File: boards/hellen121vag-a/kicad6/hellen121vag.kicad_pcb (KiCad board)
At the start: 2 copper layers, 164 x 118 mm, 70 parts, among them J1 USB_B_Mini, M1 Module-can-0.1, M10 Module-can-0.1, M11 Module-vr-0.1, M12 Module-dinput4-0.1, M2 Module-power5-0.1, M3 Module-mcu-0.1, M4 Module-input-0.1, M5 Module-knock-0.1, M6 Module-output-0.1, M7 Module-ign8-0.1, M8 Module-power12-0.1, M9 Module-wbo-0.1, P1 368255-2

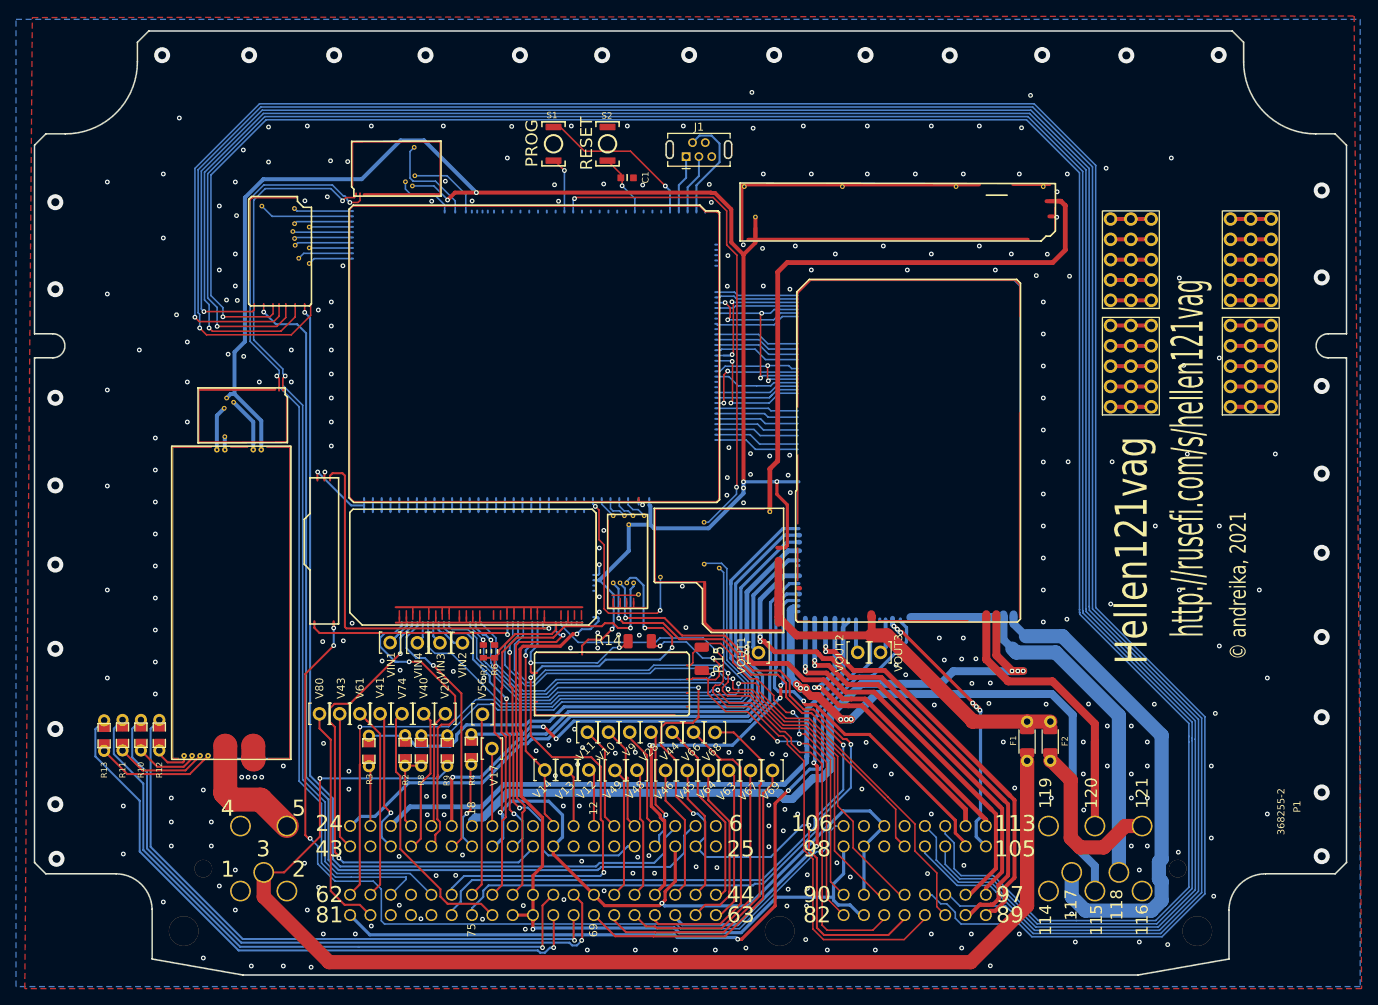
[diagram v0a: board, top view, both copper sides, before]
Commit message: Upd pcb, sch
Power5 0.2
turn connector
bridge driver is almost complete
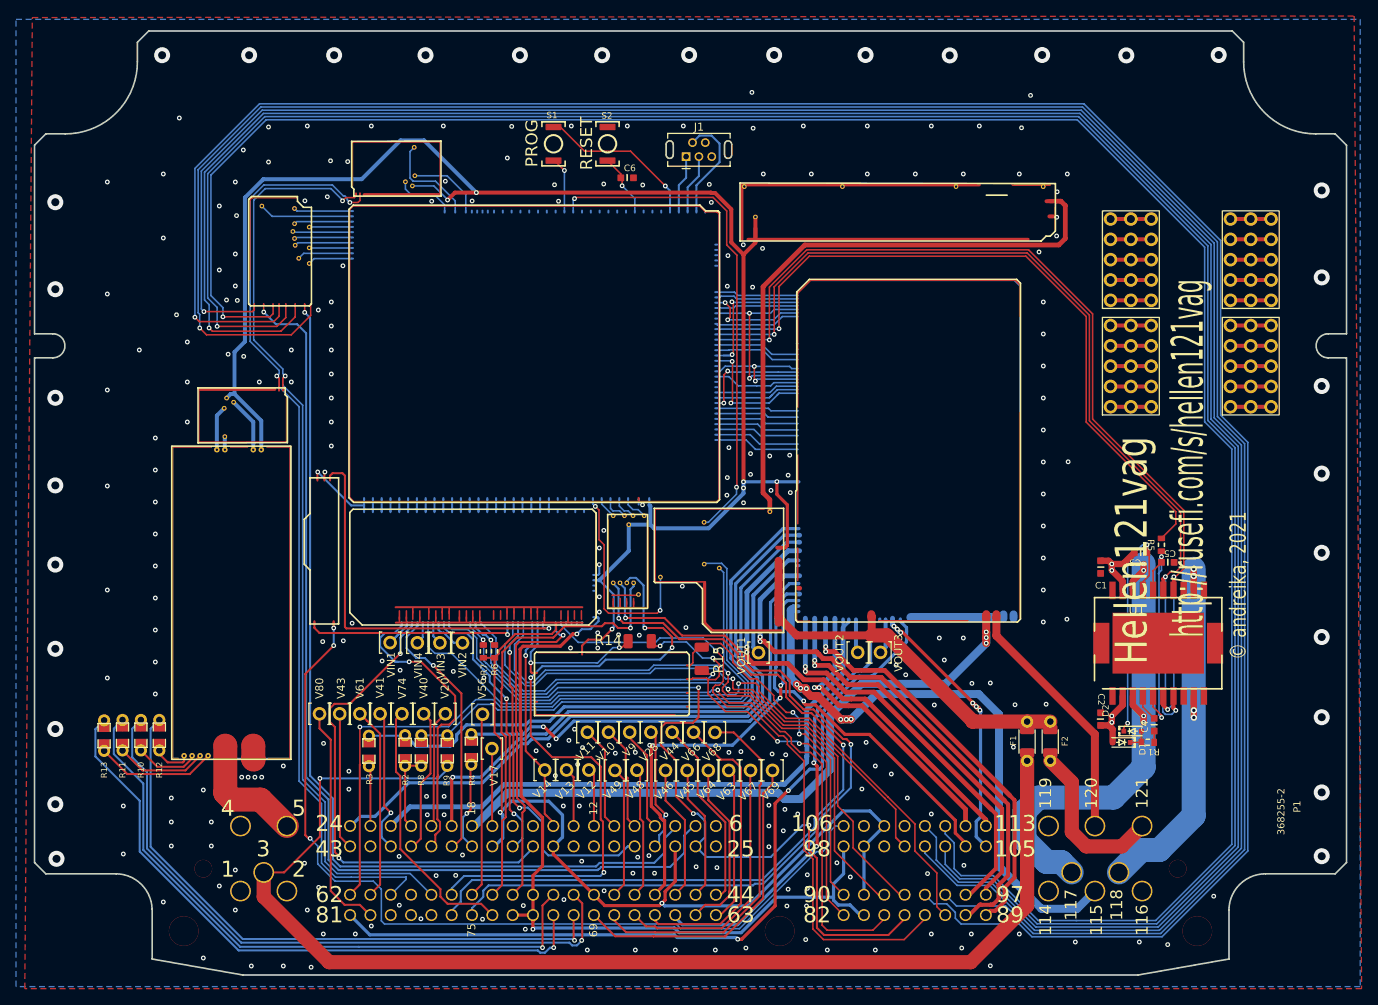
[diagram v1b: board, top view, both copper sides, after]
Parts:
- added C2: 100n, hellen-one-common:C0603, F.Cu at (179.0, 78.4)
- added C3: 220n, hellen-one-common:C0603, F.Cu at (184.0, 57.6)
- added C4: 10n, hellen-one-common:C0603, F.Cu at (185.7, 79.1)
- added C5: 5.6n, hellen-one-common:C0603, F.Cu at (187.4, 58.8)
- added C6: 100n, hellen-one-common:C0603, F.Cu at (119.8, 10.7)
- added D1: 1N4148WS, hellen-one-common:SOD-323, F.Cu at (181.6, 81.3)
- added D2: 1N4148WS, hellen-one-common:SOD-323, F.Cu at (183.0, 79.9)
- added R1: 100, hellen-one-common:R0603, F.Cu at (184.9, 81.3)
- added R5: 100k, hellen-one-common:R0603, F.Cu at (186.6, 56.6)
- added U1: L6205PD, hellen-one-common:SO20POWER, F.Cu at (186.2, 68.9)
- C1: value Cap -> 100n
- M2: value Module-power5-0.1 -> Module-power5-0.2
- R6, R7: value Res -> 2.7k
- moved C1 76.6 mm to (179.0, 59.4), turned to 90 degrees
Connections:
- net V12_RAW renamed +12V_RAW
- net V5A renamed +5VA
- C1 pad 2: /NRESET -> +12V_PROT
- M3 pad E13: unconnected-(M3-PadE13) -> /ETB_EN
- M3 pad E14: /COIL_A1 -> /+ETB
- M3 pad E15: /COIL_A2 -> /-ETB
- M3 pad E16: /VVT2_B1 -> /VVT2_B2
- M3 pad E17: /VVT2_B2 -> /VVT2_B1
- M6 pad S1: /OUT_COIL_A1 -> unconnected-(M6-PadS1)
- M6 pad S2: /OUT_COIL_A2 -> unconnected-(M6-PadS2)
- M6 pad S4: /OUT_VVT2_B1 -> /OUT_VVT2_B2
- M6 pad S5: /OUT_VVT2_B2 -> /OUT_VVT2_B1
- M6 pad W30: /VVT2_B2 -> /VVT2_B1
- M6 pad W31: /VVT2_B1 -> /VVT2_B2
- M6 pad W32: /COIL_A2 -> unconnected-(M6-PadW32)
- M6 pad W33: /COIL_A1 -> unconnected-(M6-PadW33)
- M6 pad W5: unconnected-(M6-PadW5) -> +12V_PROT
- P1 pad 117: /OUT_COIL_A1 -> /+ETB_OUT
- P1 pad 118: /OUT_COIL_A2 -> /-ETB_OUT
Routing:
- net /+ETB: track 0.00 -> 118.9 mm, vias 0 -> 3
- net /-ETB: track 0.00 -> 117.7 mm, vias 0 -> 3
- net /ETB_EN: track 0.00 -> 89.4 mm, vias 0 -> 1
- net /OUT_COIL_A1: track 61.7 -> 0.00 mm
- net /+ETB_OUT: track 0.00 -> 61.5 mm, vias 0 -> 4
- net /-ETB_OUT: track 0.00 -> 48.6 mm, vias 0 -> 4
- net /OUT_COIL_A2: track 41.6 -> 0.00 mm
- net Net-(C5-Pad2): track 0.00 -> 31.1 mm, vias 0 -> 2
- net Net-(C3-Pad1): track 0.00 -> 31.0 mm, vias 0 -> 2
- net +12V_PROT: track 0.00 -> 16.6 mm, vias 0 -> 4
- net /OUT_VVT2_B2: track 43.0 -> 31.3 mm
- net /COIL_A1: track 10.6 -> 0.00 mm
- net /COIL_A2: track 10.6 -> 0.00 mm
- net /OUT_VVT2_B1: track 92.2 -> 83.3 mm
- net /OUT_IGN3: track 274.7 -> 282.9 mm
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
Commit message: ETB driver power input
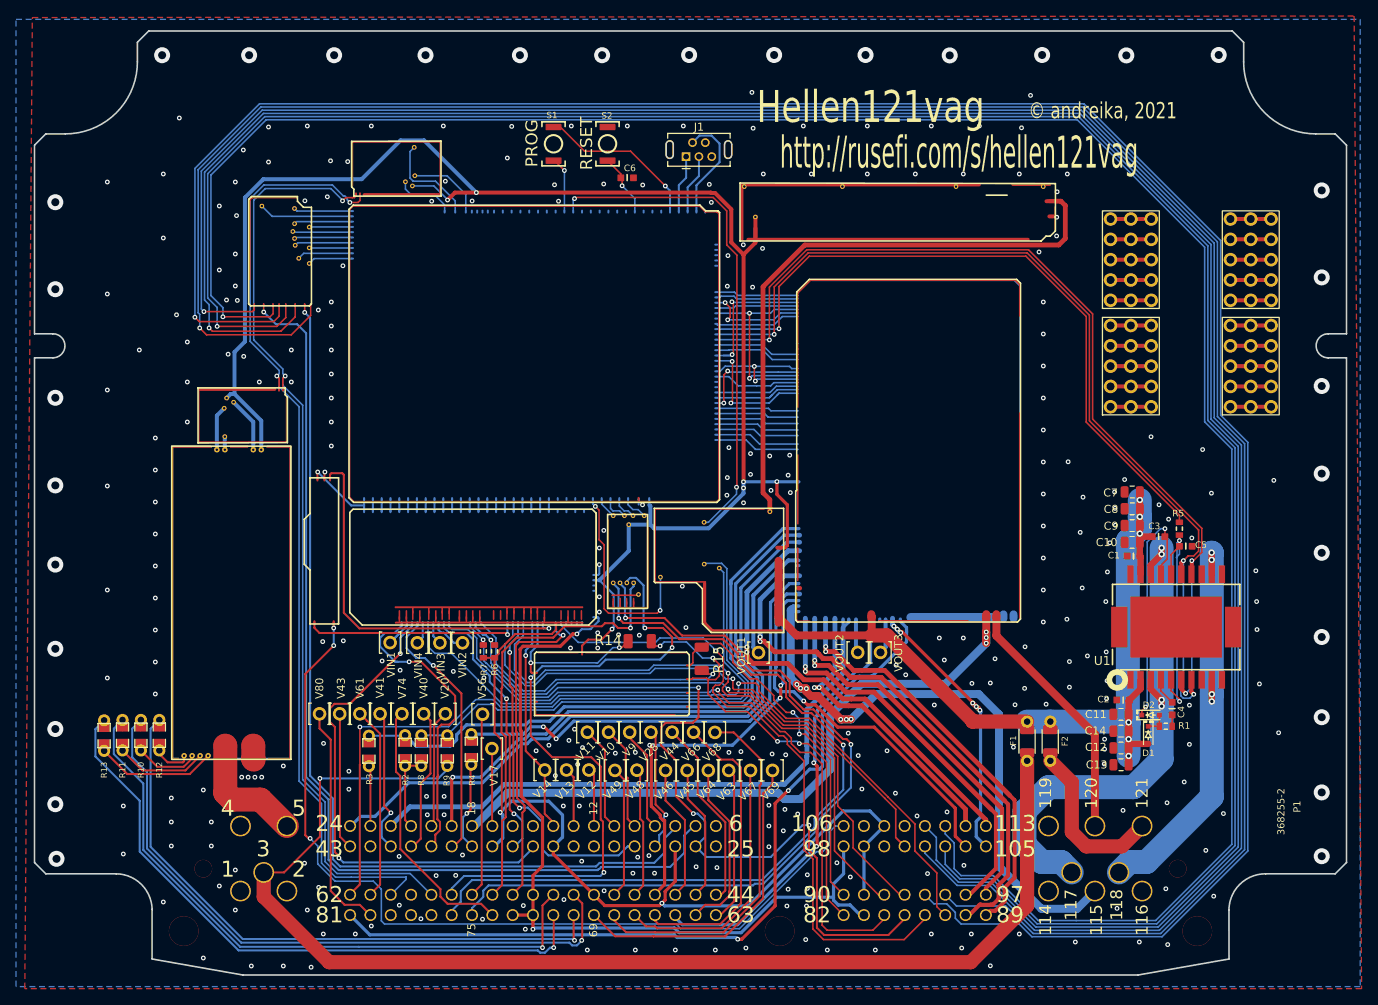
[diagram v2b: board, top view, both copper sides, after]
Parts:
- added C10: 10u, Capacitor_SMD:C_0805_2012Metric, F.Cu at (182.9, 56.3)
- added C11: 10u, Capacitor_SMD:C_0805_2012Metric, F.Cu at (181.5, 77.8)
- added C12: 10u, Capacitor_SMD:C_0805_2012Metric, F.Cu at (181.5, 82.0)
- added C13: 10u, Capacitor_SMD:C_0805_2012Metric, F.Cu at (181.5, 84.1)
- added C14: 10u, Capacitor_SMD:C_0805_2012Metric, F.Cu at (181.5, 79.9)
- added C7: 10u, Capacitor_SMD:C_0805_2012Metric, F.Cu at (182.9, 50.0)
- added C8: 10u, Capacitor_SMD:C_0805_2012Metric, F.Cu at (182.9, 52.1)
- added C9: 10u, Capacitor_SMD:C_0805_2012Metric, F.Cu at (182.9, 54.2)
- moved C1 4.34 mm to (183.1, 58.0), turned to 0 degrees
- moved C2 3.69 mm to (181.8, 76.0), turned to 0 degrees
- moved D1 3.47 mm to (184.9, 80.4), turned to -90 degrees
- moved D2 3.02 mm to (185.2, 77.9)
- moved R1 3.02 mm to (187.1, 79.3)
- moved U1 3.02 mm to (188.4, 66.9)
- moved C3 3.02 mm to (186.2, 55.6)
- moved C5 3.02 mm to (189.6, 56.8)
- moved C4 3.02 mm to (187.9, 77.1)
- moved R5 3.02 mm to (188.8, 54.6)
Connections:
- C1 pad 2: +12V_PROT -> +12V_RAW
- C2 pad 2: +12V_PROT -> +12V_RAW
- C3 pad 2: +12V_PROT -> +12V_RAW
- D1 pad 2: +12V_PROT -> +12V_RAW
- U1 pad 19: +12V_PROT -> +12V_RAW
- U1 pad 2: +12V_PROT -> +12V_RAW
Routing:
- net +12V_RAW: track 45.8 -> 113.7 mm, vias 0 -> 6
- net +12V_PROT: track 16.6 -> 0.00 mm, vias 4 -> 0
- net /+ETB_OUT: track 61.5 -> 65.5 mm
- net /-ETB_OUT: track 48.6 -> 51.5 mm
- net /ETB_EN: track 89.4 -> 86.8 mm
- net /-ETB: track 117.7 -> 116.6 mm
- net /+ETB: track 118.9 -> 117.8 mm
- net /IN_KNOCK1: track 48.5 -> 47.6 mm
- net /OUT_WASTEGATE: track 47.3 -> 48.0 mm
- net GND: vias 286 -> 329

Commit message: Improved usability
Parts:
- removed G4: PROTO_AREA, hellen-one-common:PROTO_AREA
- added BT1: BATTERY_CR2032, Battery:BatteryHolder_Keystone_1060_1x2032, F.Cu at (180.3, 32.3)
- added D3: 1N4148WS, hellen-one-common:SOD-323, F.Cu at (59.7, 15.2)
- added D4: LED-GREEN-0805, hellen-one-common:LED-0805, F.Cu at (59.7, 13.2)
- added D5: 1N4148WS, hellen-one-common:SOD-323, F.Cu at (59.7, 17.2)
- added D6: LED-GREEN-0805, hellen-one-common:LED-0805, F.Cu at (59.7, 25.2)
- added D7: LED-GREEN-0805, hellen-one-common:LED-0805, F.Cu at (59.7, 31.2)
- added D8: LED-GREEN-0805, hellen-one-common:LED-0805, F.Cu at (59.7, 19.2)
- added D9: 1N4148WS, hellen-one-common:SOD-323, F.Cu at (179.1, 15.3)
- added G5: PROTO_AREA, hellen-one-common:PROTO_AREA, F.Cu at (195.6, 37.3)
- added J2: Conn_01x01, TestPoint:TestPoint_Pad_D2.0mm, F.Cu at (63.7, 19.2)
- added J3: Conn_01x01, TestPoint:TestPoint_Pad_D2.0mm, F.Cu at (63.7, 25.2)
- added J4: Conn_01x01, TestPoint:TestPoint_Pad_D2.0mm, F.Cu at (63.7, 31.2)
- added J5: Conn_01x01, TestPoint:TestPoint_Pad_D2.0mm, F.Cu at (63.7, 37.2)
- added J6: Conn_01x01, TestPoint:TestPoint_Pad_D2.0mm, B.Cu at (59.4, 37.3)
- added J7: Conn_01x08, Connector_PinHeader_2.54mm:PinHeader_1x08_P2.54mm_Vertical, F.Cu at (119.0, 10.9)
- added R16: 4.7k, hellen-one-common:R0603-4, F.Cu at (54.7, 16.2)
- added R17: 470, hellen-one-common:R0603-4, F.Cu at (54.7, 28.2)
- moved G3 33.9 mm to (190.6, 5.78), turned to -90 degrees
- moved G1 19.1 mm to (195.6, 50.7)
- moved S1 3.41 mm to (107.2, 6.47)
- moved G2 2.06 mm to (195.6, 24.0)
- moved C6 1.90 mm to (121.2, 9.47), turned to 90 degrees
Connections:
- G3 pad 1: Net-(G3-Pad1) -> +12V
- G3 pad 10: Net-(G3-Pad10) -> GND
- G3 pad 11: Net-(G3-Pad1) -> +12V
- G3 pad 12: Net-(G3-Pad12) -> +5V
- G3 pad 13: Net-(G3-Pad13) -> +3V3
- G3 pad 14: Net-(G3-Pad14) -> GND
- G3 pad 15: Net-(G3-Pad10) -> GND
- G3 pad 2: Net-(G3-Pad12) -> +5V
- G3 pad 3: Net-(G3-Pad13) -> +3V3
- G3 pad 4: Net-(G3-Pad14) -> GND
- G3 pad 5: Net-(G3-Pad10) -> GND
- G3 pad 6: Net-(G3-Pad1) -> +12V
- G3 pad 7: Net-(G3-Pad12) -> +5V
- G3 pad 8: Net-(G3-Pad13) -> +3V3
- G3 pad 9: Net-(G3-Pad14) -> GND
- M3 pad N12: unconnected-(M3-PadN12) -> /IO1
- M3 pad N13: unconnected-(M3-PadN13) -> /IO2
- M3 pad N14: unconnected-(M3-PadN14) -> /IO3
- M3 pad N15: unconnected-(M3-PadN15) -> /IO4
- M3 pad N20: unconnected-(M3-PadN20) -> Net-(M3-PadN20)
- M3 pad N21: unconnected-(M3-PadN21) -> Net-(M3-PadN21)
- M3 pad N22: unconnected-(M3-PadN22) -> Net-(M3-PadN22)
- M3 pad N23: unconnected-(M3-PadN23) -> Net-(M3-PadN23)
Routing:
- net +3V3: track 7.01 -> 181.2 mm, vias 1 -> 2
- net +12V: track 75.5 -> 229.2 mm
- net /IN_VIGN: track 64.3 -> 162.3 mm, vias 0 -> 4
- net +5V: track 225.0 -> 294.2 mm, vias 6 -> 7
- net /VBAT: track 63.2 -> 111.7 mm, vias 2 -> 6
- net /IO1: track 0.00 -> 8.40 mm
- net /OUT_IGN3: track 282.9 -> 291.1 mm
- net /OUT_IGN5: track 286.9 -> 295.1 mm
- net /OUT_IGN6: track 295.5 -> 303.7 mm
- net /OUT_IGN1: track 287.1 -> 295.3 mm
- net /OUT_IGN8: track 295.3 -> 303.4 mm
- net /OUT_IGN4: track 294.8 -> 303.0 mm
- net Net-(M3-PadN20): track 0.00 -> 7.30 mm
- net /IO2: track 0.00 -> 7.08 mm
- net Net-(D7-Pad2): track 0.00 -> 5.59 mm
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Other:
- board text added: "+12"
- board text added: "+3.3"
- board text added: "+5"
- board text added: "G"
- board text added: "GND"
- board text added: "Vign"
- board text added: "rev. a"

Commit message: New modules schematics, baro, SWD-WBO
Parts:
- added C15: 100n, hellen-one-common:C0603, F.Cu at (97.4, 4.67)
- added G6: LOGO, hellen-one-common:LOGO, F.Cu at (193.5, 85.6)
- added J8: Conn_01x06, Connector_PinHeader_2.54mm:PinHeader_1x06_P2.54mm_Vertical, F.Cu at (58.9, 56.8)
- added J9: Conn_01x04, Connector_PinHeader_2.54mm:PinHeader_1x04_P2.54mm_Vertical, F.Cu at (108.8, 10.9)
- added R18: 4.7k, hellen-one-common:R0603, F.Cu at (100.1, 8.43)
- added R19: 4.7k, hellen-one-common:R0603, F.Cu at (102.6, 4.08)
- added U2: LPS25HB, Package_LGA:ST_HLGA-10_2.5x2.5mm_P0.6mm_LayoutBorder3x2y, F.Cu at (100.1, 4.88)
- J7: value Conn_01x08 -> Conn_01x04; footprint Connector_PinHeader_2.54mm:PinHeader_1x08_P2.54mm_Vertical -> Connector_PinHeader_2.54mm:PinHeader_1x04_P2.54mm_Vertical
- moved C6 1.70 mm to (122.9, 9.57)
- moved M10 1.53 mm to (77.4, 35.4)
- moved J7 1.52 mm to (120.5, 10.9)
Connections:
- net Net-(M3-PadN20) renamed /SPI2_SCK
- net Net-(M3-PadN21) renamed /SPI2_MISO
- net Net-(M3-PadN22) renamed /SPI2_MOSI
- net Net-(M3-PadN23) renamed /SPI2_CS
- M3 pad N18: unconnected-(M3-PadN18) -> Net-(M3-PadN18)
- M3 pad N19: unconnected-(M3-PadN19) -> Net-(M3-PadN19)
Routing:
- net Net-(M3-PadN19): track 0.00 -> 24.1 mm, vias 0 -> 1
- net Net-(M3-PadN18): track 0.00 -> 21.5 mm, vias 0 -> 1
- net Net-(J8-Pad1): track 0.00 -> 18.9 mm
- net Net-(J8-Pad2): track 0.00 -> 17.9 mm
- net Net-(J8-Pad4): track 0.00 -> 14.2 mm
- net Net-(J8-Pad5): track 0.00 -> 13.0 mm
- net +3V3: track 181.2 -> 190.5 mm
- net /NRESET: track 10.4 -> 12.6 mm
- net /SPI2_SCK: track 7.30 -> 5.51 mm
- net Net-(M10-PadV5): track 5.57 -> 7.11 mm
- net Net-(M10-PadV6): track 1.64 -> 3.17 mm
- net Net-(M10-PadV2): track 6.96 -> 8.48 mm
- net /IN_VIGN: track 162.3 -> 163.4 mm
- net /CAN-: track 118.0 -> 117.2 mm
- net /CAN+: track 119.6 -> 118.8 mm
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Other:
- board text added: "3.3"
- board text added: "CLK"
- board text added: "DIO"
- board text added: "RST"
- board text added: "SWD WBO"

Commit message: Knock audio
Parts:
- added C16: 100n, hellen-one-common:C0603, F.Cu at (80.5, 37.3)
- added C17: 10u, hellen-one-common:C0603, F.Cu at (131.7, 3.67)
- added J10: AudioJack3_SwitchTR, hellen-one-common:Jack_3.5mm_PJ-3250-5A, F.Cu at (148.2, 6.08)
- added U3: MCP6002-xSN, Package_SO:SOIC-8_3.9x4.9mm_P1.27mm, F.Cu at (81.6, 42.1)
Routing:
- net Net-(C17-Pad2): track 0.00 -> 92.7 mm, vias 0 -> 2
- net Net-(C17-Pad1): track 0.00 -> 15.6 mm
- net +5V: track 294.1 -> 302.7 mm, vias 7 -> 8
- net Net-(U3-Pad6): track 0.00 -> 3.94 mm
- net /IN_KNOCK1: track 47.6 -> 50.9 mm
- net Net-(J8-Pad1): track 18.9 -> 17.4 mm
- net GND: vias 354 -> 377
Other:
- board text added: "<- Knock audio"
